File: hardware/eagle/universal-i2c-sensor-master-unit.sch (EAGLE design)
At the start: 30 parts, among them X1 22-23-2041, X10 22-23-2041, X11 22-23-2041, X12 22-23-2021, X13 22-23-2021, X14 22-23-2021, X2 22-23-2041, X3 22-23-2041, X4 22-23-2041, X5 22-23-2041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

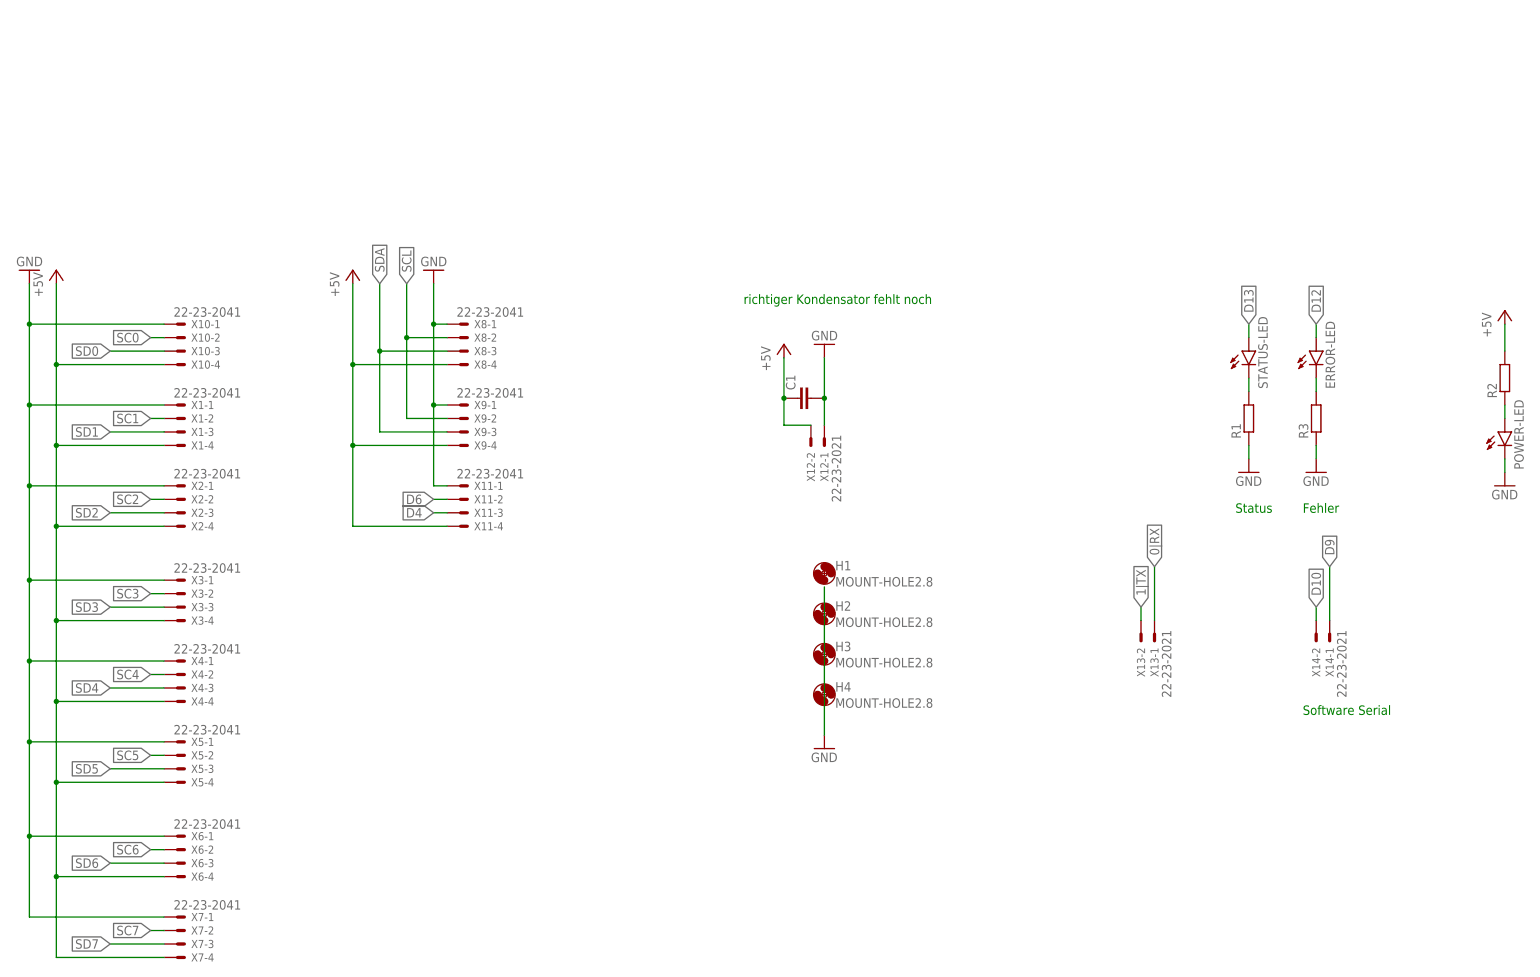
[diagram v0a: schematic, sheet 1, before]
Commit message: Layout Reworked & Lables
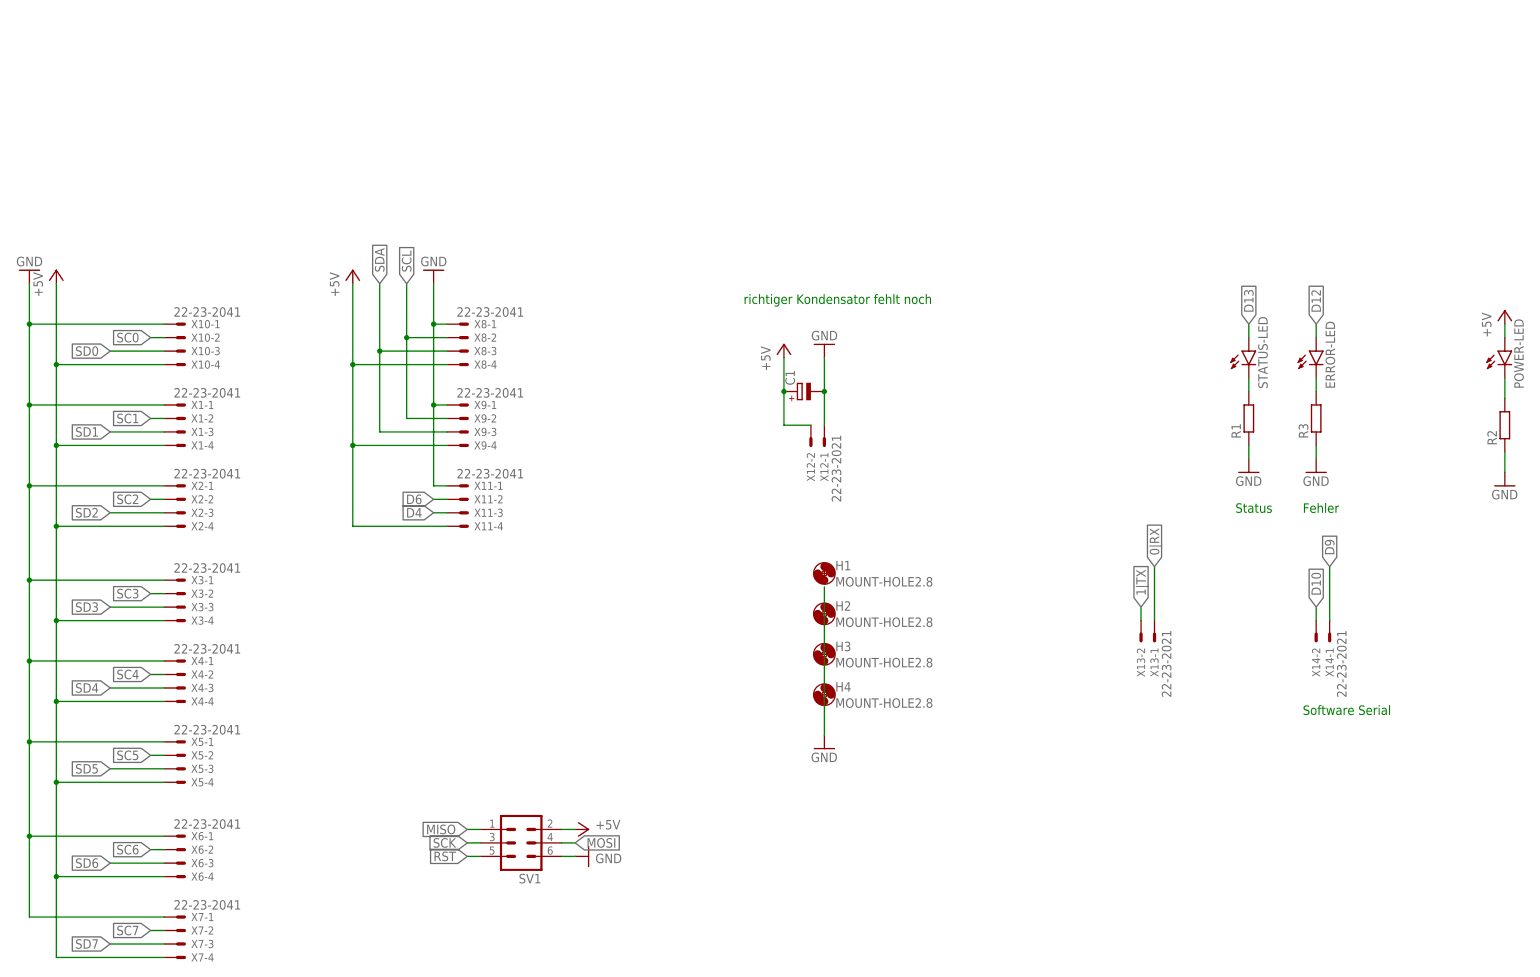
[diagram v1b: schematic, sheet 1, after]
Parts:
- added SV1: (no value), con-lstb:MA03-2
- C1: device rcl:C-EU025-025X050 -> rcl:CPOL-EUE2.5-6
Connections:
- removed net MIS0: JP1.13
- removed net RST2: JP1.1
- new net MISO: JP1.13, SV1.1
- new net RST: JP1.1, SV1.5
- net +5V: now also C1.+, POWER-LED.A, SV1.2; no longer C1.1, R2.2
- net GND: now also C1.-, R2.1, SV1.6; no longer C1.2, POWER-LED.C
- net MOSI: now also SV1.4
- net N$2: now also POWER-LED.C, R2.2; no longer POWER-LED.A, R2.1
- net SCK: now also SV1.3
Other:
- moved on the sheet: POWER-LED, R2

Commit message: SMD Jumper for Soft / Hard I2C
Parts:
- added SJ1, SJ2, SJ3, SJ4: (no value), jumper:SJ2W
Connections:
- new net SCL_EXTRA: SJ4.2, X11-3.S
- new net SCL_SENSORS: JP4.4, SJ2.2, X8-2.S, X9-2.S
- new net SDA_EXTRA: SJ3.2, X11-2.S
- new net SDA_SENSORS: JP4.3, SJ1.2, X8-3.S, X9-3.S
- net D4: now also SJ1.3, SJ3.3; no longer X11-3.S
- net D6: now also SJ2.3, SJ4.3; no longer X11-2.S
- net SCL: now also SJ2.1, SJ4.1; no longer JP4.4, X8-2.S, X9-2.S
- net SDA: now also SJ1.1, SJ3.1; no longer JP4.3, X8-3.S, X9-3.S
